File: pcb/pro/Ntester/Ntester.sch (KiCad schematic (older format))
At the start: 1 part

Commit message: added rest of files
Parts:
- removed C?: C_Small, symbol Device:C_Small
- added C2, C5, C6: B45196-H2227-M409, Capacitor_Tantalum_SMD:CP_EIA-7343-31_Kemet-D, symbol Device:CP_Small
- added C22, C23: 0603B104M500CT, Resistor_SMD:R_0603_1608Metric, symbol Device:C_Small
- added C4: 885012006007, Resistor_SMD:R_0603_1608Metric, symbol Device:C_Small
- added C7: DNP, Capacitor_Tantalum_SMD:CP_EIA-7343-31_Kemet-D, symbol Device:CP_Small
- added D1, D2: BAS116LT1G, Package_TO_SOT_SMD:SOT-23, symbol Device:D_Schottky_AAK
- added FB1: 742792651, Resistor_SMD:R_0603_1608Metric, symbol Device:Ferrite_Bead_Small
- added J1, J5, J6: Conn_Coaxial, Connector_Coaxial:BNC_TEConnectivity_1478204_Vertical, symbol Connector:Conn_Coaxial
- added J2: Conn_01x02_Male, Connector_PinHeader_2.54mm:PinHeader_1x02_P2.54mm_Vertical, symbol Connector:Conn_01x02_Male
- added J4: 67996-408HLF, Connector_PinHeader_2.54mm:PinHeader_2x04_P2.54mm_Vertical, symbol Connector_Generic:Conn_02x04_Odd_Even
- added JP1: CAL_FUSE, Jumper:SolderJumper-2_P1.3mm_Bridged_Pad1.0x1.5mm, symbol Device:Jumper_NC_Small
- added R3: RMCF0603FT499R, Resistor_SMD:R_0603_1608Metric, symbol Device:R_Small
- added R7: RHC2512FT4R99, Resistor_SMD:R_2512_6332Metric, symbol Device:R_Small
- added R8: CRM2512-JW-470ELF, Resistor_SMD:R_2512_6332Metric, symbol Device:R_Small
- added R9: CR1206-FX-4990ELF, Resistor_SMD:R_1206_3216Metric, symbol Device:R_Small
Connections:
- new net: J4.4 (Pin_4), R8.1
- new net: J4.6 (Pin_6), R7.1
- new net: J4.2 (Pin_2), R9.1
- new net: J4.8 (Pin_8), JP1.1
- new net: C2.1, C4.1, C5.1, C6.1, C7.1, D1.1 (A), D2.1 (A), FB1.1, J4.1 (Pin_1), J4.3 (Pin_3), J4.5 (Pin_5), J4.7 (Pin_7)
- new net: FB1.2, J1.1 (In), J2.1 (Pin_1)
- new net +5V: C22.1, C23.1, D1.3 (K)
- new net -5V: D2.3 (K)
- new net GND: C22.2, C23.2, C4.2, J1.2 (Ext), J2.2 (Pin_2), J5.2 (Ext), J6.2 (Ext), JP1.2, R3.2, R7.2, R8.2, R9.2
- new net InputStage/IN_SIG: C2.2, C5.2, C6.2, C7.2, R3.1
- no-connect marks 0 -> 2
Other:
- note added: "0R - cal only\n5R -> 2A -> 20W\n50R -> 200mA -> 2W\n499R -> 20mA -> 0.2W"
- note added: "220uF/10V"
- note added: "499R"
- note added: "5V nom\n10V abs MAX\n"
- note added: "68p"
- note added: "TODO:\ncheck polarization of caps\nchange value of caps 100uF->220uF\nchange resitors 06->04"

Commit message: " alomost" finalized layout
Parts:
- removed C2, C5, C6: B45196-H2227-M409, Capacitor_Tantalum_SMD:CP_EIA-7343-31_Kemet-D, symbol Device:CP_Small
- removed C22, C23: 0603B104M500CT, Resistor_SMD:R_0603_1608Metric, symbol Device:C_Small
- removed C4: 885012006007, Resistor_SMD:R_0603_1608Metric, symbol Device:C_Small
- removed C7: DNP, Capacitor_Tantalum_SMD:CP_EIA-7343-31_Kemet-D, symbol Device:CP_Small
- removed D1, D2: BAS116LT1G, Package_TO_SOT_SMD:SOT-23, symbol Device:D_Schottky_AAK
- removed FB1: 742792651, Resistor_SMD:R_0603_1608Metric, symbol Device:Ferrite_Bead_Small
- removed J1: Conn_Coaxial, Connector_Coaxial:BNC_TEConnectivity_1478204_Vertical, symbol Connector:Conn_Coaxial
- removed J2: Conn_01x02_Male, Connector_PinHeader_2.54mm:PinHeader_1x02_P2.54mm_Vertical, symbol Connector:Conn_01x02_Male
- removed J4: 67996-408HLF, Connector_PinHeader_2.54mm:PinHeader_2x04_P2.54mm_Vertical, symbol Connector_Generic:Conn_02x04_Odd_Even
- removed JP1: CAL_FUSE, Jumper:SolderJumper-2_P1.3mm_Bridged_Pad1.0x1.5mm, symbol Device:Jumper_NC_Small
- removed R3: RMCF0603FT499R, Resistor_SMD:R_0603_1608Metric, symbol Device:R_Small
- removed R7: RHC2512FT4R99, Resistor_SMD:R_2512_6332Metric, symbol Device:R_Small
- removed R8: CRM2512-JW-470ELF, Resistor_SMD:R_2512_6332Metric, symbol Device:R_Small
- removed R9: CR1206-FX-4990ELF, Resistor_SMD:R_1206_3216Metric, symbol Device:R_Small
- added H1, H2, H3, H4: M3.5, MountingHole:MountingHole_3.5mm_Pad_Via, symbol Mechanical:MountingHole_Pad
- added J1: Conn_01x02_Male, Connector_PinHeader_2.54mm:PinHeader_1x02_P2.54mm_Vertical, symbol Connector:Conn_01x02_Male
- added J2, J3: Conn_Coaxial, Connector_Coaxial:BNC_TEConnectivity_1478204_Vertical, symbol Connector:Conn_Coaxial
- added J7: 36503505S 36003500S, RF_Shielding:Wuerth_36503505_50x50mm, symbol Device:RF_Shield_Two_Pieces
- added JP2, JP3, JP4, JP5: GND_SHIELD, Jumper:SolderJumper-2_P1.3mm_Open_TrianglePad1.0x1.5mm, symbol Device:Jumper_NC_Small
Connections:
- net GND: now also J1.2 (Pin_2), J2.2 (Ext), J3.2 (Ext), J7.1 (Shield), JP2.2, JP3.2, JP4.2, JP5.2
- net GainBlock/1MHZ_OUT: now also J6.1 (In)
- net GainBlock/WB_OUT: now also J5.1 (In)
- new net: H4.1, JP5.1
- new net: H3.1, JP4.1
- new net: H2.1, JP3.1
- new net: H1.1, JP2.1
- new net InputStage/IN_STG: J1.1 (Pin_1), J2.1 (In), J3.1 (In)
- no-connect marks 2 -> 0
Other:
- note removed: "0R - cal only\n5R -> 2A -> 20W\n50R -> 200mA -> 2W\n499R -> 20mA -> 0.2W"
- note removed: "220uF/10V"
- note removed: "499R"
- note removed: "68p"
- moved on the sheet: J5, J6

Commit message: layout finalized
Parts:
- added TP1, TP4: TestPoint, TestPoint:TestPoint_THTPad_D1.0mm_Drill0.5mm, symbol Connector:TestPoint
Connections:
- net GND: now also TP4.1
- net InputAmplifier/IN_AMP: now also TP1.1
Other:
- note added: "Do zamówienia:\nLT1818\nLT6231"
- note removed: "TODO:\ncheck polarization of caps\nchange value of caps 100uF->220uF\nchange resitors 06->04"
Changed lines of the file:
@@
 $Descr A4 11693 8268
 encoding utf-8
-Sheet 1 5
-Title ""
+Sheet 1 8
+Title "Power Supply Noise Tester"
 Date ""
-Rev ""
-Comp ""
+Rev "1.0"
+Comp "Paweł Woźny"
 Comment1 ""
 Comment2 ""
@@
 F3 "OUT_AMP" I R 7550 2250 50
 $EndSheet
-Text Notes 8000 1150 0    157  ~ 0
-TODO:\ncheck polarization of caps\nchange value of caps 100uF->220uF\nchange resitors 06->04
-Wire Notes Line
-	5950 3500 7500 3500
-Wire Notes Line
-	7500 3500 7500 2750
-Wire Notes Line
-	7500 2750 5950 2750
-Wire Notes Line
-	5950 2700 5950 3500
-Wire Notes Line
-	5850 4550 7400 4550
-Wire Notes Line
-	7400 4550 7400 3800
-Wire Notes Line
-	7400 3800 5850 3800
-Wire Notes Line
-	5850 3750 5850 4550
-Wire Notes Line
-	5850 5600 7400 5600
-Wire Notes Line
-	7400 5600 7400 4850
-Wire Notes Line
-	7400 4850 5850 4850
-Wire Notes Line
-	5850 4800 5850 5600
-Wire Notes Line
-	5350 5200 5850 5200
 $Sheet
 S 8100 3200 1400 750
@@
 F4 "1MHZ_OUT" I R 9500 3750 50
 $EndSheet
-Wire Wire Line
-	5450 3200 5750 3200
 Wire Wire Line
 	5450 2250 5900 2250
@@
 	7550 2250 7850 2250
 Wire Wire Line
-	7850 2250 7850 3550
-Wire Wire Line
 	7850 3550 8100 3550
 $Sheet
@@
 Wire Wire Line
 	1950 3700 2900 3700
-Wire Wire Line
-	5450 2250 5450 3200
-Wire Wire Line
-	5450 3200 5450 3700
-Wire Wire Line
-	4300 3700 5450 3700
-Connection ~ 5450 3200
 $Sheet
 S 3400 6550 1550 650
@@
 Wire Wire Line
 	1700 6900 1700 7000
+Text Notes 12200 1950 0    118  ~ 0
+Do zamówienia:\nLT1818\nLT6231
+$Sheet
+S 5850 3000 1600 750
+U 5BE7BD5E
+F0 "LNA1" 50
+F1 "LNA1.sch" 50
+F2 "IN_AMP" I L 5850 3300 50
+F3 "OUT_AMP" I R 7450 3350 50
+$EndSheet
+Wire Wire Line
+	7850 2250 7850 3350
+Wire Wire Line
+	5450 2250 5450 3300
+Wire Wire Line
+	7450 3350 7850 3350
+Connection ~ 7850 3350
+Wire Wire Line
+	7850 3350 7850 3550
+Wire Wire Line
+	5850 3300 5450 3300
+Connection ~ 5450 3300
+Wire Wire Line
+	5450 3300 5450 3700
+$Comp
+L Connector:TestPoint TP?
+U 1 1 5BDDBE16
+P 1250 6936
+AR Path="/5BCA1695/5BDDBE16" Ref="TP?"  Part="1"
+AR Path="/5BE53A35/5BDDBE16" Ref="TP?"  Part="1"
+AR Path="/5BDDBE16" Ref="TP4"  Part="1"
+F 0 "TP4" H 1308 7008 50  0000 L CNN
+F 1 "TestPoint" H 1308 6963 50  0001 L CNN
+F 2 "TestPoint:TestPoint_THTPad_D1.0mm_Drill0.5mm" H 1450 6936 50  0001 C CNN
+F 3 "~" H 1450 6936 50  0001 C CNN
+	1    1250 6936
+	1    0    0    -1
+$EndComp
+$Comp
+L power:GND #PWR?
+U 1 1 5BDDBE1C
+P 1250 7036
+AR Path="/5BCA1695/5BDDBE1C" Ref="#PWR?"  Part="1"
+AR Path="/5BE0B501/5BDDBE1C" Ref="#PWR?"  Part="1"
+AR Path="/5BE53A35/5BDDBE1C" Ref="#PWR?"  Part="1"
+AR Path="/5BDDBE1C" Ref="#PWR0147"  Part="1"
+F 0 "#PWR0147" H 1250 6786 50  0001 C CNN
+F 1 "GND" H 1255 6863 50  0000 C CNN
+F 2 "" H 1250 7036 50  0001 C CNN
+F 3 "" H 1250 7036 50  0001 C CNN
+	1    1250 7036
+	1    0    0    -1
+$EndComp
+Wire Wire Line
+	1250 7036 1250 6936
+Wire Wire Line
+	4300 3700 4850 3700
+Wire Wire Line
+	4850 3700 4850 3450
+Connection ~ 4850 3700
+Wire Wire Line
+	4850 3700 5450 3700
+$Comp
+L Connector:TestPoint TP?
+U 1 1 5BDD2090
+P 4850 3450
+AR Path="/5BCA1695/5BDD2090" Ref="TP?"  Part="1"
+AR Path="/5BE53A35/5BDD2090" Ref="TP?"  Part="1"
+AR Path="/5BDD2090" Ref="TP1"  Part="1"
+F 0 "TP1" H 4908 3522 50  0000 L CNN
+F 1 "TestPoint" H 4908 3477 50  0001 L CNN
+F 2 "TestPoint:TestPoint_THTPad_D1.0mm_Drill0.5mm" H 5050 3450 50  0001 C CNN
+F 3 "~" H 5050 3450 50  0001 C CNN
+	1    4850 3450
+	1    0    0    -1
+$EndComp
+$Sheet
+S 5850 4100 1600 700
+U 5BDD458C
+F0 "LNA2" 50
+F1 "LNA2.sch" 50
+F2 "IN_AMP" I L 5850 4450 50
+F3 "OUT_AMP" I R 7450 4450 50
+$EndSheet
+Wire Wire Line
+	5850 4450 5450 4450
+Wire Wire Line
+	5450 4450 5450 3700
+Connection ~ 5450 3700
+Wire Wire Line
+	7450 4450 7850 4450
+Wire Wire Line
+	7850 4450 7850 3550
+Connection ~ 7850 3550
+$Sheet
+S 5850 5050 1600 650
+U 5BE154B7
+F0 "LNA3" 50
+F1 "LNA3.sch" 50
+F2 "IN_AMP" I L 5850 5350 50
+F3 "OUT_AMP" I R 7450 5400 50
+$EndSheet
+Wire Wire Line
+	5850 5350 5450 5350
+Wire Wire Line
+	5450 5350 5450 4450
+Connection ~ 5450 4450
+Wire Wire Line
+	7450 5400 7850 5400
+Wire Wire Line
+	7850 5400 7850 4450
+Connection ~ 7850 4450
+$Comp
+L Graphic:Logo_Open_Hardware_Small #LOGO1
+U 1 1 5BE54ADD
+P 10750 6850
+F 0 "#LOGO1" H 10750 7125 50  0001 C CNN
+F 1 "Logo_Open_Hardware_Small" H 10750 6625 50  0001 C CNN
+F 2 "Symbol:OSHW-Logo2_7.3x6mm_SilkScreen" H 10750 6850 50  0001 C CNN
+F 3 "~" H 10750 6850 50  0001 C CNN
+	1    10750 6850
+	1    0    0    -1
+$EndComp
 $EndSCHEMATC

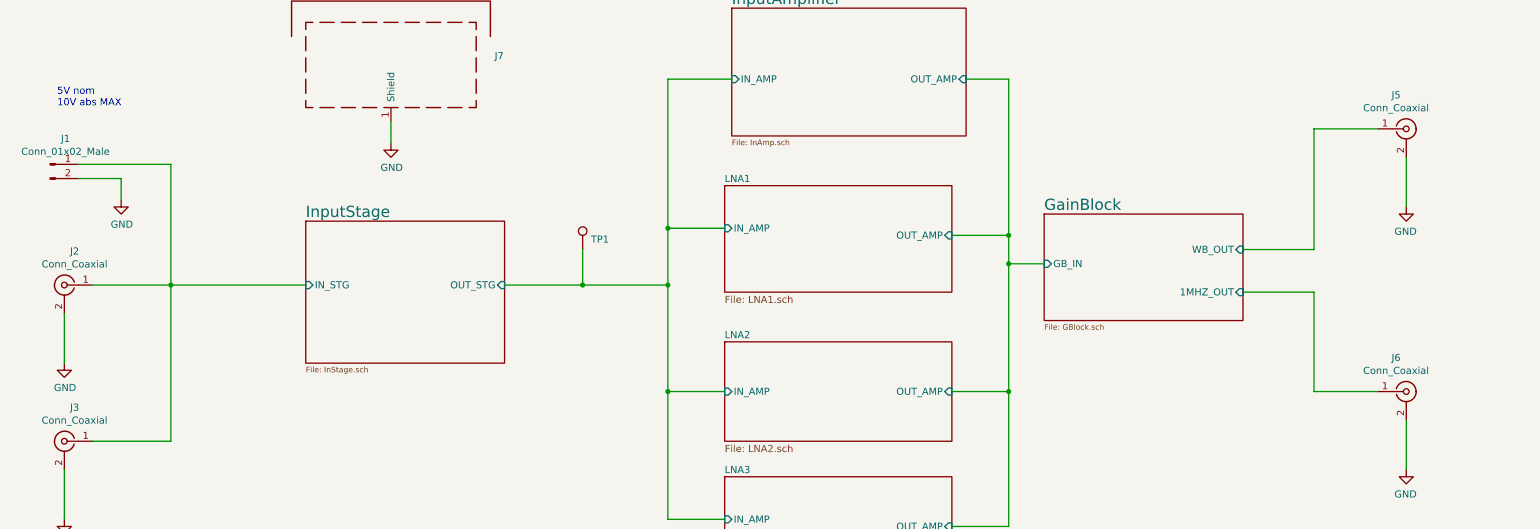
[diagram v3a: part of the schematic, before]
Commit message: BOM was updated
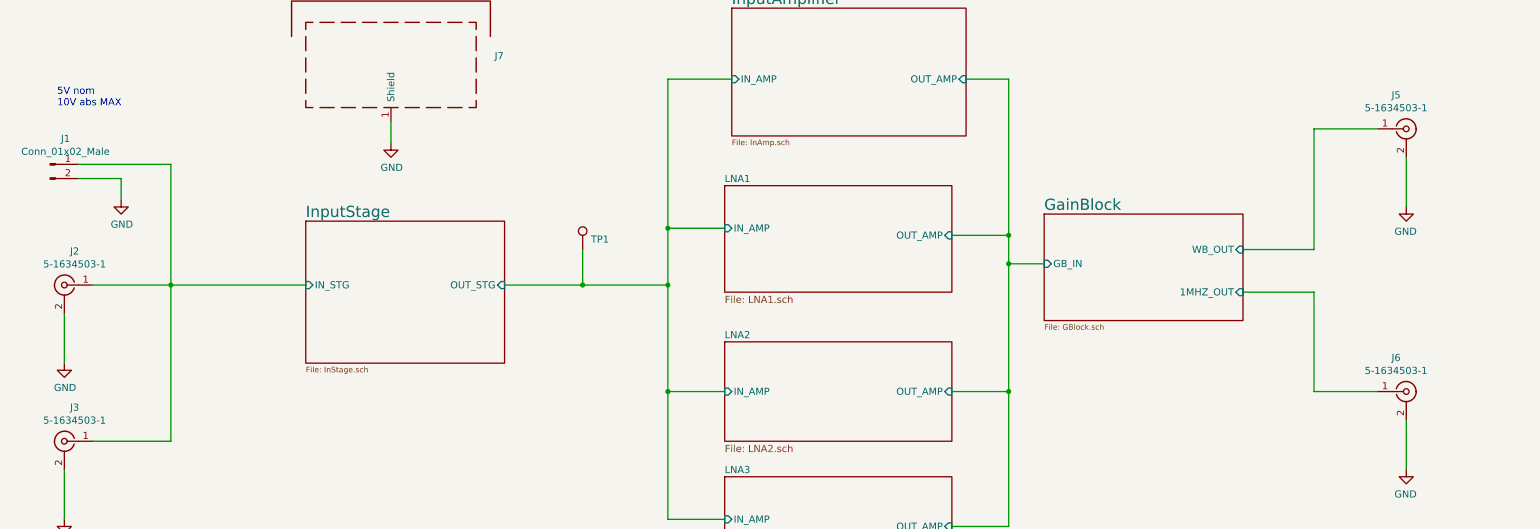
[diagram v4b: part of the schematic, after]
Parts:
- J2, J3, J5, J6: value Conn_Coaxial -> 5-1634503-1
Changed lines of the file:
@@
 P 10650 2600
 F 0 "J5" H 10578 2838 50  0000 C CNN
-F 1 "Conn_Coaxial" H 10578 2747 50  0000 C CNN
+F 1 "5-1634503-1" H 10578 2747 50  0000 C CNN
 F 2 "Connector_Coaxial:BNC_TEConnectivity_1478204_Vertical" H 10650 2600 50  0001 C CNN
 F 3 " ~" H 10650 2600 50  0001 C CNN
@@
 P 10650 4450
 F 0 "J6" H 10578 4688 50  0000 C CNN
-F 1 "Conn_Coaxial" H 10578 4597 50  0000 C CNN
+F 1 "5-1634503-1" H 10578 4597 50  0000 C CNN
 F 2 "Connector_Coaxial:BNC_TEConnectivity_1478204_Vertical" H 10650 4450 50  0001 C CNN
 F 3 " ~" H 10650 4450 50  0001 C CNN
@@
 P 1200 3700
 F 0 "J2" H 1128 3938 50  0000 C CNN
-F 1 "Conn_Coaxial" H 1128 3847 50  0000 C CNN
+F 1 "5-1634503-1" H 1128 3847 50  0000 C CNN
 F 2 "Connector_Coaxial:BNC_TEConnectivity_1478204_Vertical" H 1200 3700 50  0001 C CNN
 F 3 " ~" H 1200 3700 50  0001 C CNN
@@
 P 1200 4800
 F 0 "J3" H 1128 5038 50  0000 C CNN
-F 1 "Conn_Coaxial" H 1128 4947 50  0000 C CNN
+F 1 "5-1634503-1" H 1128 4947 50  0000 C CNN
 F 2 "Connector_Coaxial:BNC_TEConnectivity_1478204_Vertical" H 1200 4800 50  0001 C CNN
 F 3 " ~" H 1200 4800 50  0001 C CNN
